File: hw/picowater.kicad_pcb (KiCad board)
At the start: 2 copper layers, 92.9 x 55.5 mm, 45 parts, among them J1 +12V, J10 Batt TP, J11 Humidity, J12 Ultrasound, J2 Power In, J3 +5V Pins, J4 UART, J5 Power Out, J6 JST-PH2 Bat, J7 GPIO2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

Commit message: [hw] update pcb
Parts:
- removed D2: green, LED_THT:LED_D3.0mm
- added D4: LED, LED_SMD:LED_0603_1608Metric_Pad1.05x0.95mm_HandSolder, F.Cu at (69.9, 71.0)
- BT1: footprint Battery:Battery_Panasonic_CR2032-VS1N_Vertical_CircularHoles -> Lunasys_Library:CR2032_Vertical_TE_1775485-1
- D1: moved to F.Cu
- R3: value 330 -> 220; footprint Resistor_SMD:R_1206_3216Metric_Pad1.30x1.75mm_HandSolder -> Resistor_SMD:R_0402_1005Metric; moved to F.Cu
- SW1: footprint Button_Switch_SMD:SW_Push_SPST_NO_Alps_SKRK -> Button_Switch_THT:SW_PUSH_6mm
- moved R3 7.02 mm to (73.3, 71.0), turned to 0 degrees
- moved D1 6.49 mm to (103.9, 74.9), turned to -90 degrees
- moved BT1 5.66 mm to (66.0, 78.0)
- moved SW1 3.98 mm to (62.5, 115.3), turned to 180 degrees
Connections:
- R3 pad 2: GND -> Net-(U1-GPIO0)
- U1 pad 1: Net-(D2-A) -> Net-(U1-GPIO0)
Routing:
- net Net-(D1-K): track 14.2 -> 6.13 mm
- net Net-(D2-A): track 6.46 -> 0.00 mm
- net +5V: track 71.1 -> 77.3 mm, vias 0 -> 1
- net Net-(U1-GPIO0): track 0.00 -> 6.05 mm
- net 1~{PRE}: track 21.0 -> 24.5 mm
- net GND: track 27.3 -> 29.2 mm
- net Net-(D4-A): track 3.16 -> 2.00 mm
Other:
- board size 92.9 x 55.5 mm -> 93.3 x 55.5 mm

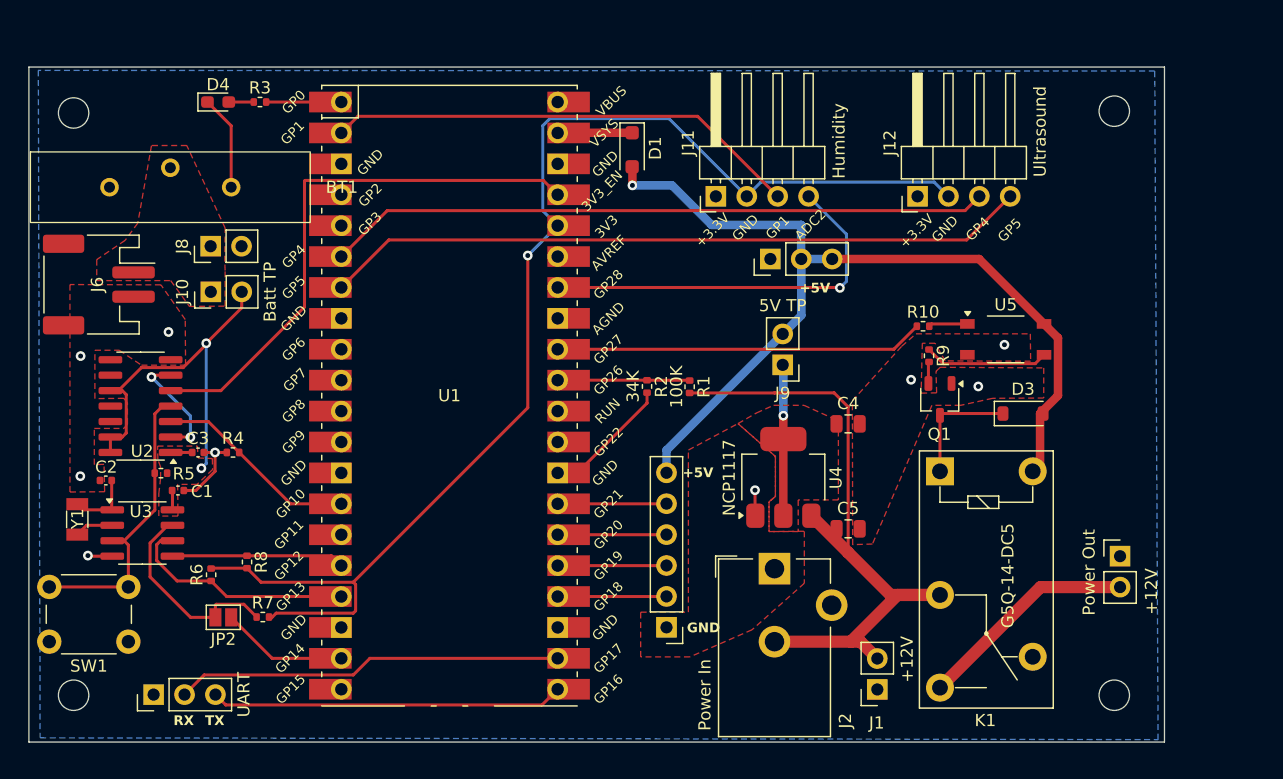
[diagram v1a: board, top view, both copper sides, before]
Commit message: [pcb] fixes following v0.9
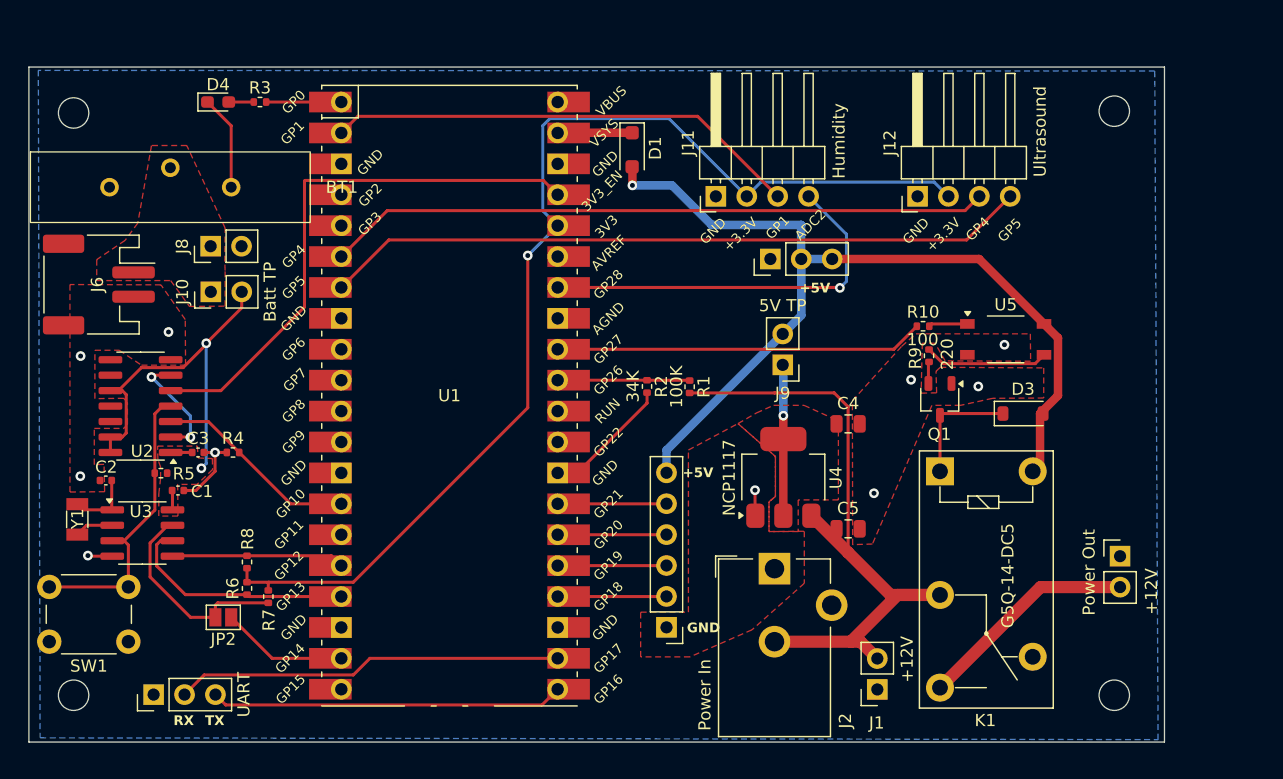
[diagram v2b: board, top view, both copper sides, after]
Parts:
- moved R6 3.16 mm to (72.2, 111.0)
- moved R7 1.73 mm to (74.0, 111.7), turned to 90 degrees
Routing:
- net +3.3V: track 104.1 -> 92.8 mm
- net CLKOUT: track 16.8 -> 17.4 mm
- net GND: vias 9 -> 10

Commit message: [pcb] fixes
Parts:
- removed Q1: S8050, Package_TO_SOT_SMD:TSOT-23
- added Q2: BC817, Package_TO_SOT_SMD:SOT-23, F.Cu at (129.2, 95.8)
- R10: value 100 -> 220
- R3: value 220 -> 4.7K
- R7: footprint Resistor_SMD:R_0402_1005Metric -> Resistor_SMD:R_0805_2012Metric
- moved U5 8.86 mm to (125.8, 89.3)
- moved R10 7.81 mm to (120.0, 88.5), turned to 90 degrees
- moved D1 7.19 mm to (107.3, 81.3)
- moved R9 1.98 mm to (130.2, 92.5)
- moved J3 1.63 mm to (113.7, 84.3)
- moved R8 1.10 mm to (71.2, 108.8)
- moved R6 1.10 mm to (71.2, 111.0)
- moved D3 0.75 mm to (135.3, 96.6)
- moved R7 0.18 mm to (74.0, 111.5)
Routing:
- net +5V: track 77.3 -> 66.0 mm, vias 1 -> 2
- net +3.3V: track 92.8 -> 81.5 mm, vias 1 -> 2
- net Net-(R9-Pad1): track 10.2 -> 1.95 mm
- net GPIO27: track 30.3 -> 23.3 mm
- net Net-(D1-K): track 6.13 -> 12.2 mm
- net ADC2: track 32.2 -> 26.6 mm
- net Net-(D3-K): track 10.1 -> 9.28 mm
- net GPIO4: track 54.5 -> 55.2 mm
- net Net-(R10-Pad2): track 3.21 -> 2.63 mm
- net GND: vias 10 -> 9

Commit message: better use of the new rtc
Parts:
- U2: footprint Package_SO:SOIC-14_3.9x8.7mm_P1.27mm -> Package_SO:SO-14_5.3x10.2mm_P1.27mm
- U5: value TLP160G -> ~; footprint Package_SO:MFSOP6-4_4.4x3.6mm_P1.27mm -> Package_DIP:SMDIP-4_W7.62mm
- moved U2 0.98 mm to (62.5, 96.0)
- moved R9 0.72 mm to (130.2, 93.3)
- moved Q2 0.57 mm to (129.2, 96.4)
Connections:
- U5 pad 3: GND -> Net-(R9-Pad1)
- U5 pad 4: Net-(R9-Pad1) -> +5V
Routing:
- net +5V: track 66.0 -> 67.4 mm
- net GND: track 29.2 -> 28.0 mm
- net Net-(R10-Pad2): track 2.63 -> 1.97 mm
- net Net-(D3-K): track 9.28 -> 8.73 mm

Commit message: [pcb] add internal temp sensor
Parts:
- added R11: 4K7, Capacitor_SMD:C_0402_1005Metric, F.Cu at (73.5, 96.9)
- added R12: 4K7, Capacitor_SMD:C_0402_1005Metric, F.Cu at (75.4, 94.2)
- added U6: MCP9808_MSOP, Package_SO:MSOP-8_3x3mm_P0.65mm, F.Cu at (71.5, 94.3)
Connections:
- U1 pad 10: unconnected-(U1-GPIO7-Pad10) -> I2C1-SCL
- U1 pad 9: GPIO6 -> I2C1-SDA
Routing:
- net +3.3V: track 81.5 -> 114.5 mm
- net I2C1-SDA: track 0.00 -> 13.6 mm
- net I2C1-SCL: track 0.00 -> 6.73 mm
- net GND: track 28.0 -> 33.3 mm, vias 9 -> 11
- net 3V3_EN: track 45.5 -> 46.4 mm

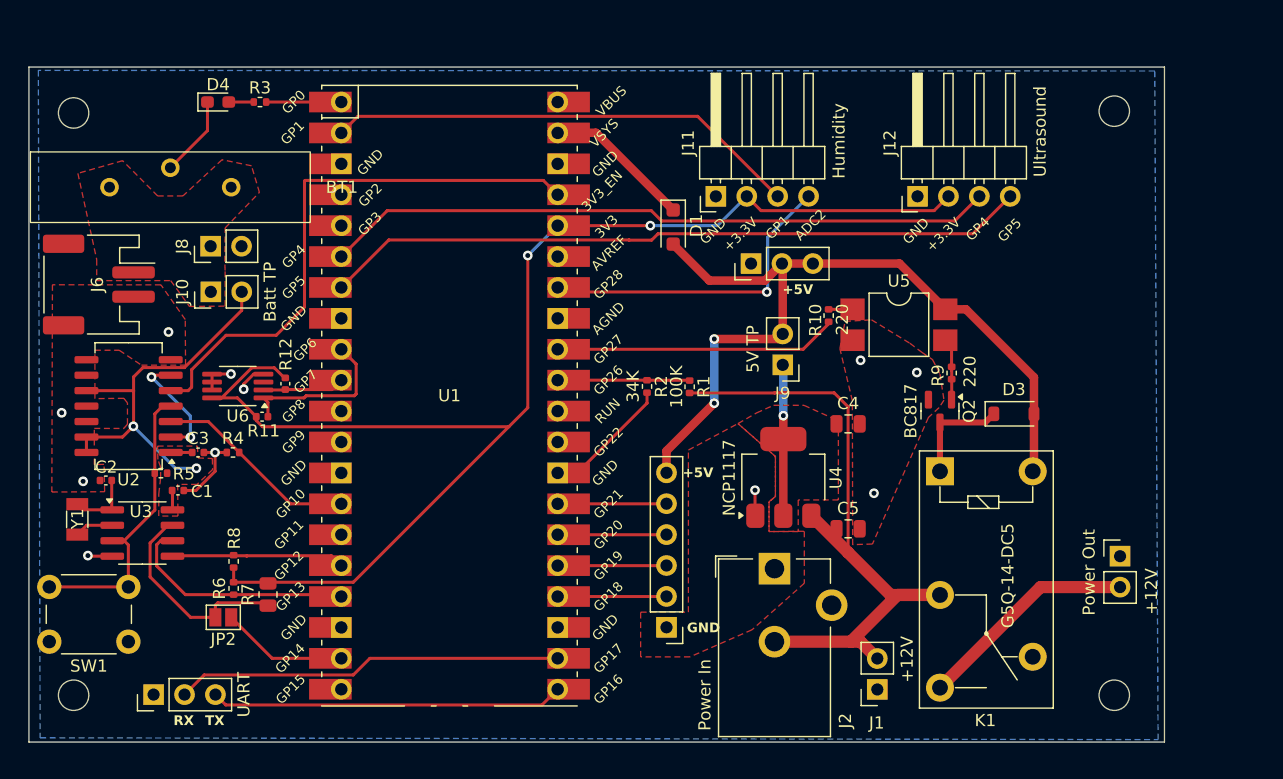
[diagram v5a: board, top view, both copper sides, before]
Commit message: [pcb] lots of fixes and simplification
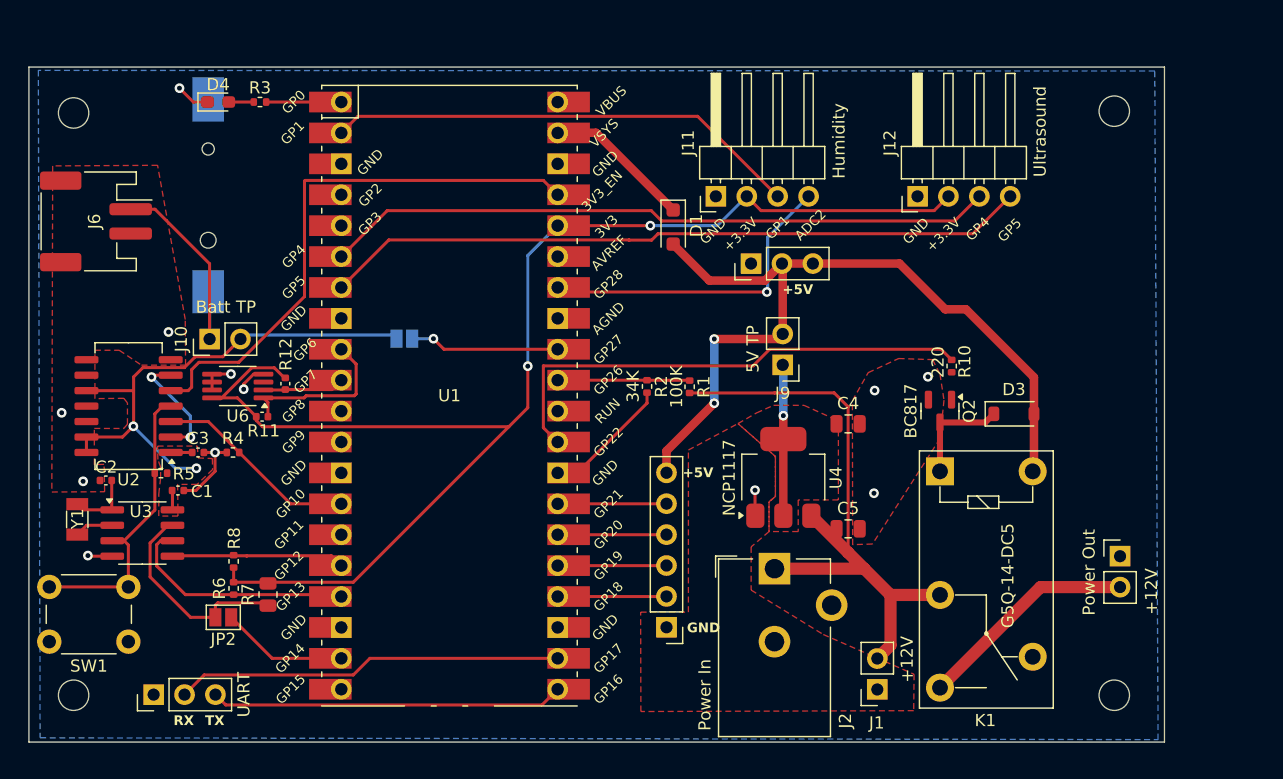
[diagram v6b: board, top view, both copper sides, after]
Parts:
- removed BT1: Battery_Cell, Lunasys_Library:CR2032_Vertical_TE_1775485-1
- removed J8: Alt-Bat, Connector_PinHeader_2.54mm:PinHeader_1x02_P2.54mm_Vertical
- removed R9: 220, Resistor_SMD:R_0402_1005Metric
- removed U5: ~, Package_DIP:SMDIP-4_W7.62mm
- added BT2: 3V Cell, cell:MPD_BC501SM-TR, B.Cu at (69.1, 78.4)
- added JP3: JP_ADC_BAT, Jumper:SolderJumper-2_P1.3mm_Open_Pad1.0x1.5mm, B.Cu at (85.2, 90.5)
- moved R10 10.9 mm to (130.2, 92.7), turned to -90 degrees
- moved J6 5.20 mm to (59.8, 80.8)
- moved J10 3.88 mm to (69.2, 90.5)
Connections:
- net Net-(BT1-+) renamed RAW_BAT+
- J2 pad 1: GND -> +12V
- J2 pad 2: +12V -> GND
- R10 pad 1: GPIO27 -> GPIO22
- R10 pad 2: Net-(R10-Pad2) -> Net-(Q2-B)
- U1 pad 29: unconnected-(U1-GPIO22-Pad29) -> GPIO22
- U1 pad 32: GPIO27 -> ADC1
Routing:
- net GPIO22: track 0.00 -> 41.2 mm
- net GPIO27: track 23.3 -> 0.00 mm
- net RAW_BAT+: track 0.00 -> 18.5 mm
- net ADC1: track 0.00 -> 12.3 mm, vias 0 -> 1
- net +BATT: track 36.1 -> 46.6 mm
- net +12V: track 56.7 -> 51.8 mm
- net GND: track 33.3 -> 29.4 mm, vias 11 -> 12
- net Net-(R9-Pad1): track 2.26 -> 0.00 mm
- net Net-(R10-Pad2): track 1.97 -> 0.00 mm
- net Net-(Q2-B): track 1.83 -> 0.00 mm
- net 3V3_EN: track 46.4 -> 45.8 mm
- removed copper zone on F.Cu, net RAW_BAT+

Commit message: [hw] new PCB with RJ45 as connector and other changes + case
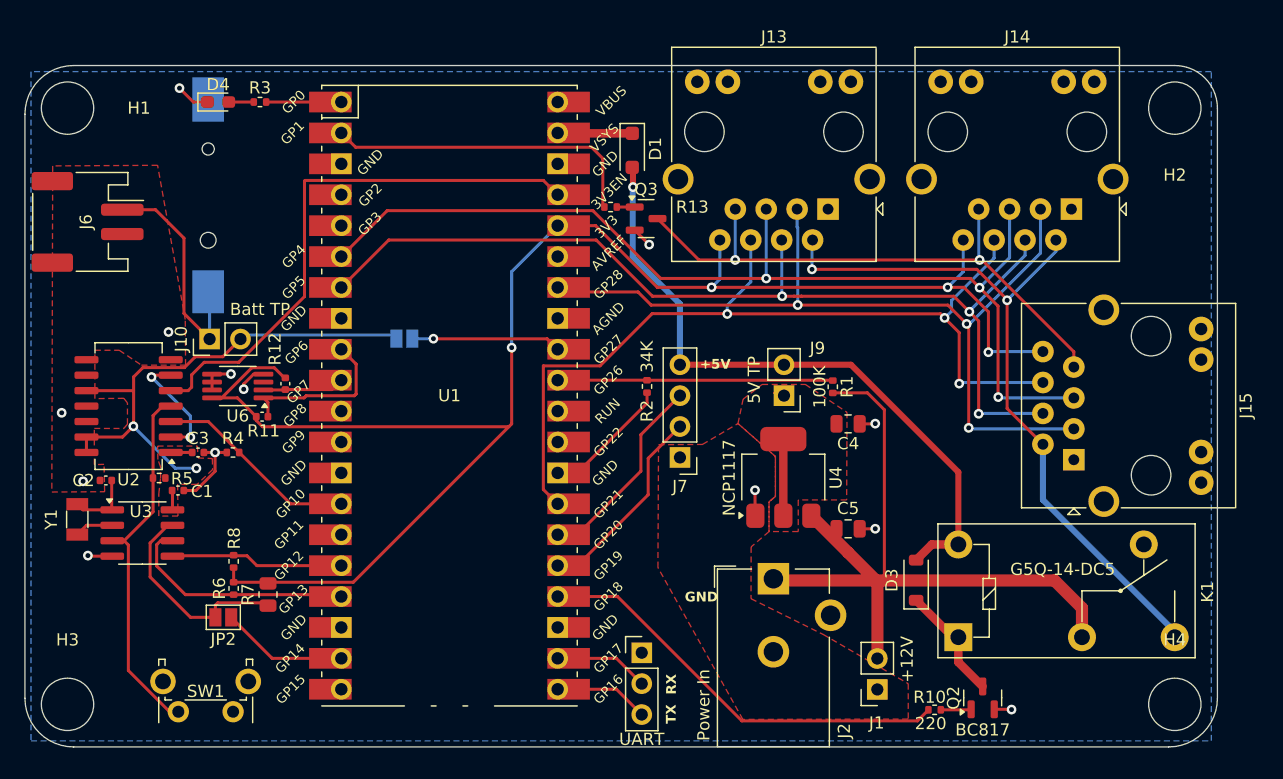
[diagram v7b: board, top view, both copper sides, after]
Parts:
- removed J11: Humidity, Connector_PinHeader_2.54mm:PinHeader_1x04_P2.54mm_Horizontal
- removed J12: Ultrasound, Connector_PinHeader_2.54mm:PinHeader_1x04_P2.54mm_Horizontal
- removed J3: +5V Pins, Connector_PinHeader_2.54mm:PinHeader_1x03_P2.54mm_Vertical
- removed J5: Power Out, Connector_PinHeader_2.54mm:PinHeader_1x02_P2.54mm_Vertical
- added J13: RJ45, Connector_RJ:RJ45_BEL_SS74301-00x_Vertical, F.Cu at (120.0, 79.8)
- added J14: RJ45, Connector_RJ:RJ45_BEL_SS74301-00x_Vertical, F.Cu at (140.0, 79.8)
- added J15: RJ45, Connector_RJ:RJ45_BEL_SS74301-00x_Vertical, F.Cu at (140.2, 100.4)
- added Q3: BC817, Package_TO_SOT_SMD:SOT-23, F.Cu at (105.0, 80.6)
- added R13: 220, Resistor_SMD:R_0402_1005Metric, F.Cu at (102.1, 79.6)
- BT2: footprint cell:MPD_BC501SM-TR -> cell:MPD_BC501SM-TR_custom
- H1, H2, H3, H4: footprint MountingHole:MountingHole_2.5mm -> MountingHole:MountingHole_4.3mm_M4
- J7: footprint Connector_PinHeader_2.54mm:PinHeader_1x06_P2.54mm_Vertical -> Connector_PinHeader_2.54mm:PinHeader_1x04_P2.54mm_Vertical
- SW1: footprint Button_Switch_THT:SW_PUSH_6mm -> Button_Switch_THT:SW_Tactile_SPST_Angled_PTS645Vx31-2LFS
- moved J4 40.3 mm to (104.7, 116.3), turned to 0 degrees
- moved R10 28.3 mm to (128.8, 121.0), turned to 0 degrees
- moved Q2 23.8 mm to (132.7, 120.0), turned to 90 degrees
- moved D3 15.9 mm to (127.2, 110.3), turned to 90 degrees
- moved J7 14.0 mm to (107.8, 100.2)
- moved K1 13.7 mm to (130.7, 115.0), turned to 0 degrees
- moved R1 11.8 mm to (120.4, 94.4)
- moved SW1 10.4 mm to (71.1, 121.1)
- moved D1 7.14 mm to (103.9, 75.0)
- moved H4 5.03 mm to (148.5, 120.5)
- moved H2 4.98 mm to (148.5, 71.5)
- moved J9 2.53 mm to (116.4, 95.1)
- moved H3 0.90 mm to (57.5, 120.5)
- moved J2 0.83 mm to (115.5, 110.2)
- moved J6 0.69 mm to (59.1, 80.8)
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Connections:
- J7 pad 4: Net-(J7-Pin_4) -> +5V
- K1 pad 3: Net-(J5-Pin_2) -> PUMP+12V
- R10 pad 1: GPIO22 -> GPIO18
- U1 pad 24: Net-(J7-Pin_2) -> GPIO18
- U1 pad 25: Net-(J7-Pin_3) -> Net-(J7-Pin_2)
- U1 pad 26: Net-(J7-Pin_4) -> Net-(J7-Pin_3)
- U1 pad 27: Net-(J7-Pin_5) -> GPIO21
- U1 pad 29: GPIO22 -> unconnected-(U1-GPIO22-Pad29)
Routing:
- net GPIO21: track 0.00 -> 74.5 mm, vias 0 -> 3
- net PUMP+12V: track 0.00 -> 59.6 mm, vias 0 -> 2
- net EXT_POWER-: track 0.00 -> 48.4 mm, vias 0 -> 2
- net ADC2: track 26.6 -> 72.1 mm, vias 1 -> 3
- net GPIO22: track 41.2 -> 0.00 mm
- net GPIO18: track 0.00 -> 35.1 mm
- net GPIO4: track 55.2 -> 85.7 mm, vias 0 -> 3
- net /RX: track 31.9 -> 7.77 mm
- net GPIO5: track 58.1 -> 82.1 mm, vias 0 -> 3
- net /TX: track 29.0 -> 7.77 mm
- net +3.3V: track 114.5 -> 135.1 mm, vias 2 -> 4
- net Net-(J5-Pin_2): track 18.2 -> 0.00 mm
- net +5V: track 67.4 -> 54.4 mm, vias 2 -> 1
- net GPIO1: track 39.1 -> 26.3 mm
- net ADC0: track 10.9 -> 22.6 mm
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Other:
- board size 93.3 x 55.5 mm -> 98 x 56 mm
- board text added: "v1.0"
- board text removed: "+12V"
- board text removed: "+3.3V"
- board text removed: "ADC2"
- board text removed: "GP1"
- board text removed: "GP4"
- board text removed: "GP5"
- board text removed: "v0.9"
